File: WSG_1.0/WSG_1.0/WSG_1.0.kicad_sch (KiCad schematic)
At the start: 0 parts

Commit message: working on esp, power and signal done
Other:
- added sheet WSG_ADC (untitled.kicad_sch)
- added sheet WSG_ESP (WSG_ESP.kicad_sch)
- added sheet WSG_Power-Memory (WSG_ADC.kicad_sch)
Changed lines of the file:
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@@
 	(generator_version "10.0")
 	(paper "A4")
+	(sheet
+		(at 45.72 96.52)
+		(size 57.15 30.48)
+		(exclude_from_sim no)
+		(in_bom yes)
+		(on_board yes)
+		(dnp no)
+		(fields_autoplaced yes)
+		(stroke
+			(width 0.1524)
+			(type solid)
+		)
+		(fill
+			(color 0 0 0 0)
+		)
+		(property "Sheetname" "WSG_Power-Memory"
+			(at 45.72 95.8084 0)
+			(show_name no)
+			(do_not_autoplace no)
+			(effects
+				(font
+					(size 1.27 1.27)
+				)
+				(justify left bottom)
+			)
+		)
+		(property "Sheetfile" "WSG_ADC.kicad_sch"
+			(at 45.72 127.5846 0)
+			(show_name no)
+			(do_not_autoplace no)
+			(effects
+				(font
+					(size 1.27 1.27)
+				)
+				(justify left top)
+			)
+		)
+		(instances
+			(project "WSG_1.0"
+				(path "/cb65811d-b245-4002-a5a3-eef29f2c4ddb"
+					(page "4")
+				)
+			)
+		)
+	)
+	(sheet
+		(at 148.59 60.96)
+		(size 68.58 36.83)
+		(exclude_from_sim no)
+		(in_bom yes)
+		(on_board yes)
+		(dnp no)
+		(fields_autoplaced yes)
+		(stroke
+			(width 0.1524)
+			(type solid)
+		)
+		(fill
+			(color 0 0 0 0)
+		)
+		(property "Sheetname" "WSG_ESP"
+			(at 148.59 60.2484 0)
+			(show_name no)
+			(do_not_autoplace no)
+			(effects
+				(font
+					(size 1.27 1.27)
+				)
+				(justify left bottom)
+			)
+		)
+		(property "Sheetfile" "WSG_ESP.kicad_sch"
+			(at 148.59 98.3746 0)
+			(show_name no)
+			(do_not_autoplace no)
+			(effects
+				(font
+					(size 1.27 1.27)
+				)
+				(justify left top)
+			)
+		)
+		(instances
+			(project "WSG_1.0"
+				(path "/cb65811d-b245-4002-a5a3-eef29f2c4ddb"
+					(page "3")
+				)
+			)
+		)
+	)
+	(sheet
+		(at 54.61 57.15)
+		(size 54.61 29.21)
+		(exclude_from_sim no)
+		(in_bom yes)
+		(on_board yes)
+		(dnp no)
+		(fields_autoplaced yes)
+		(stroke
+			(width 0.1524)
+			(type solid)
+		)
+		(fill
+			(color 0 0 0 0)
+		)
+		(property "Sheetname" "WSG_ADC"
+			(at 54.61 56.4384 0)
+			(show_name no)
+			(do_not_autoplace no)
+			(effects
+				(font
+					(size 1.27 1.27)
+				)
+				(justify left bottom)
+			)
+		)
+		(property "Sheetfile" "untitled.kicad_sch"
+			(at 54.61 86.9446 0)
+			(show_name no)
+			(do_not_autoplace no)
+			(effects
+				(font
+					(size 1.27 1.27)
+				)
+				(justify left top)
+			)
+		)
+		(instances
+			(project "WSG_1.0"
+				(path "/cb65811d-b245-4002-a5a3-eef29f2c4ddb"
+					(page "2")
+				)
+			)
+		)
+	)
 	(sheet_instances
 		(path "/"

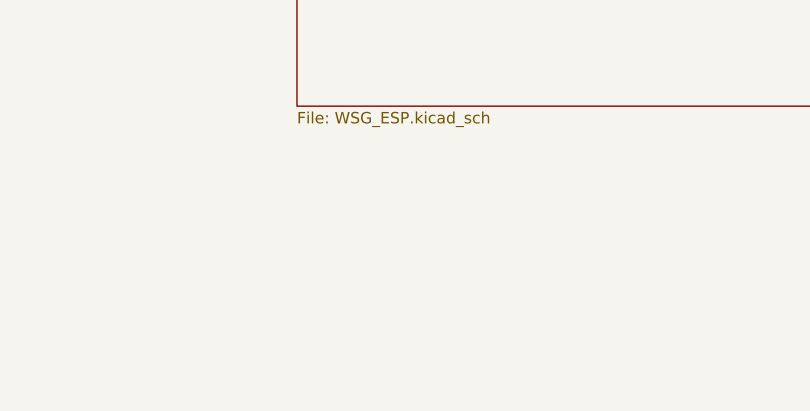
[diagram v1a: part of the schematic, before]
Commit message: added mounting holes, usb esd
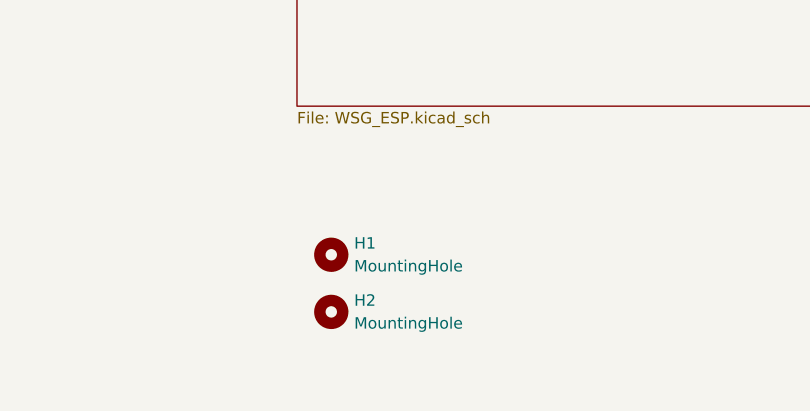
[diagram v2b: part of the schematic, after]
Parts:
- added H1, H2: MountingHole, symbol Mechanical:MountingHole
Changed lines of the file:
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@@
 	(generator_version "10.0")
 	(paper "A4")
+	(symbol
+		(lib_id "Mechanical:MountingHole")
+		(at 152.4 114.3 0)
+		(unit 1)
+		(body_style 1)
+		(exclude_from_sim no)
+		(in_bom no)
+		(on_board yes)
+		(in_pos_files yes)
+		(dnp no)
+		(fields_autoplaced yes)
+		(property "Reference" "H1"
+			(at 154.94 113.0299 0)
+			(show_name no)
+			(do_not_autoplace no)
+			(effects
+				(font
+					(size 1.27 1.27)
+				)
+				(justify left)
+			)
+		)
+		(property "Value" "MountingHole"
+			(at 154.94 115.5699 0)
+			(show_name no)
+			(do_not_autoplace no)
+			(effects
+				(font
+					(size 1.27 1.27)
+				)
+				(justify left)
+			)
+		)
+		(property "Footprint" ""
+			(at 152.4 114.3 0)
+			(hide yes)
+			(show_name no)
+			(do_not_autoplace no)
+			(effects
+				(font
+					(size 1.27 1.27)
+				)
+			)
+		)
+		(property "Datasheet" ""
+			(at 152.4 114.3 0)
+			(hide yes)
+			(show_name no)
+			(do_not_autoplace no)
+			(effects
+				(font
+					(size 1.27 1.27)
+				)
+			)
+		)
+		(property "Description" "Mounting Hole without connection"
+			(at 152.4 114.3 0)
+			(hide yes)
+			(show_name no)
+			(do_not_autoplace no)
+			(effects
+				(font
+					(size 1.27 1.27)
+				)
+			)
+		)
+		(instances
+			(project "WSG_1.0"
+				(path "/cb65811d-b245-4002-a5a3-eef29f2c4ddb"
+					(reference "H1")
+					(unit 1)
+				)
+			)
+		)
+	)
+	(symbol
+		(lib_id "Mechanical:MountingHole")
+		(at 152.4 120.65 0)
+		(unit 1)
+		(body_style 1)
+		(exclude_from_sim no)
+		(in_bom no)
+		(on_board yes)
+		(in_pos_files yes)
+		(dnp no)
+		(fields_autoplaced yes)
+		(property "Reference" "H2"
+			(at 154.94 119.3799 0)
+			(show_name no)
+			(do_not_autoplace no)
+			(effects
+				(font
+					(size 1.27 1.27)
+				)
+				(justify left)
+			)
+		)
+		(property "Value" "MountingHole"
+			(at 154.94 121.9199 0)
+			(show_name no)
+			(do_not_autoplace no)
+			(effects
+				(font
+					(size 1.27 1.27)
+				)
+				(justify left)
+			)
+		)
+		(property "Footprint" ""
+			(at 152.4 120.65 0)
+			(hide yes)
+			(show_name no)
+			(do_not_autoplace no)
+			(effects
+				(font
+					(size 1.27 1.27)
+				)
+			)
+		)
+		(property "Datasheet" ""
+			(at 152.4 120.65 0)
+			(hide yes)
+			(show_name no)
+			(do_not_autoplace no)
+			(effects
+				(font
+					(size 1.27 1.27)
+				)
+			)
+		)
+		(property "Description" "Mounting Hole without connection"
+			(at 152.4 120.65 0)
+			(hide yes)
+			(show_name no)
+			(do_not_autoplace no)
+			(effects
+				(font
+					(size 1.27 1.27)
+				)
+			)
+		)
+		(instances
+			(project "WSG_1.0"
+				(path "/cb65811d-b245-4002-a5a3-eef29f2c4ddb"
+					(reference "H2")
+					(unit 1)
+				)
+			)
+		)
+	)
 	(sheet
 		(at 45.72 96.52)

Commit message: forgot to commit, started layout and started implementing sophie's/cyan's feedback for the schematic
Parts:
- H1, H2: footprint (none) -> MountingHole:MountingHole_3.2mm_M3
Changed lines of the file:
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@@
 			)
 		)
-		(property "Footprint" ""
+		(property "Footprint" "MountingHole:MountingHole_3.2mm_M3"
 			(at 152.4 114.3 0)
 			(hide yes)
@@
 			)
 		)
-		(property "Footprint" ""
+		(property "Footprint" "MountingHole:MountingHole_3.2mm_M3"
 			(at 152.4 120.65 0)
 			(hide yes)

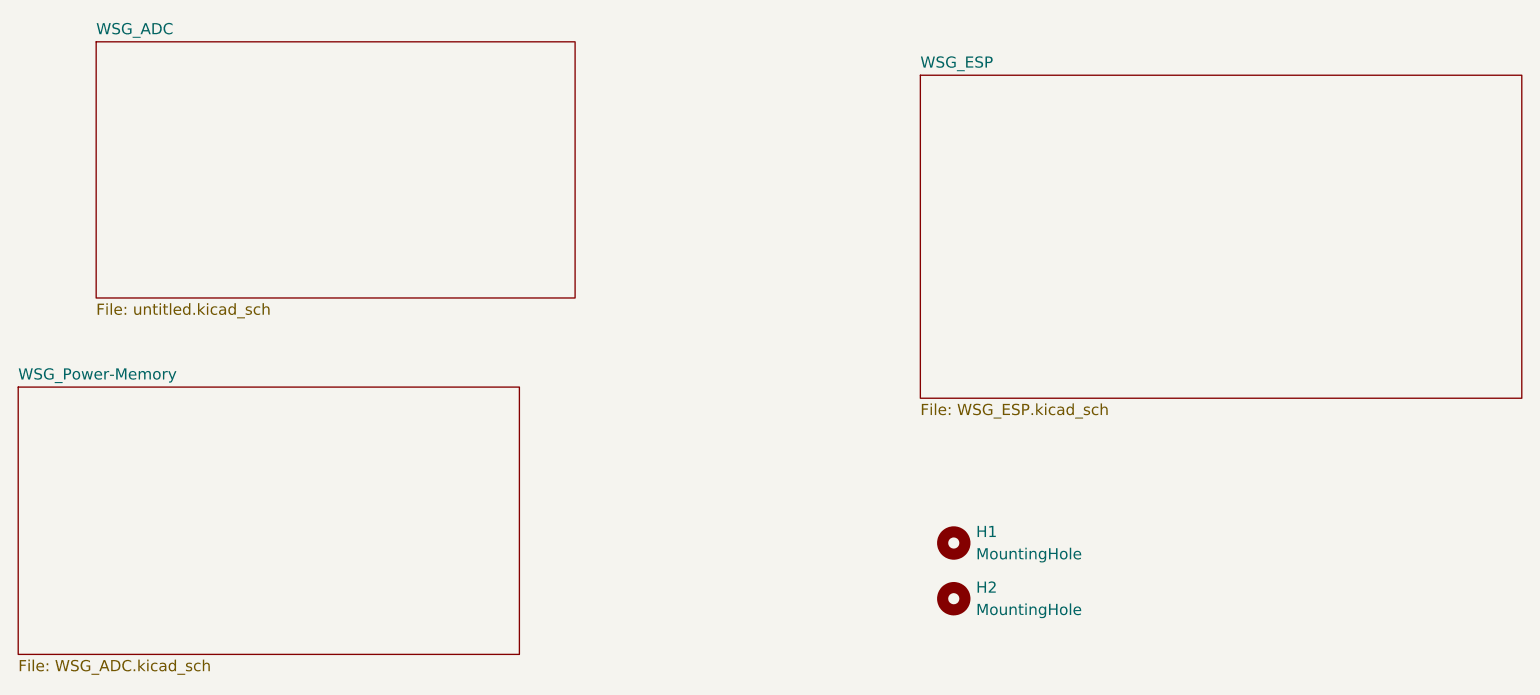
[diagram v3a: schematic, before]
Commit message: new layout started, clusters almost done
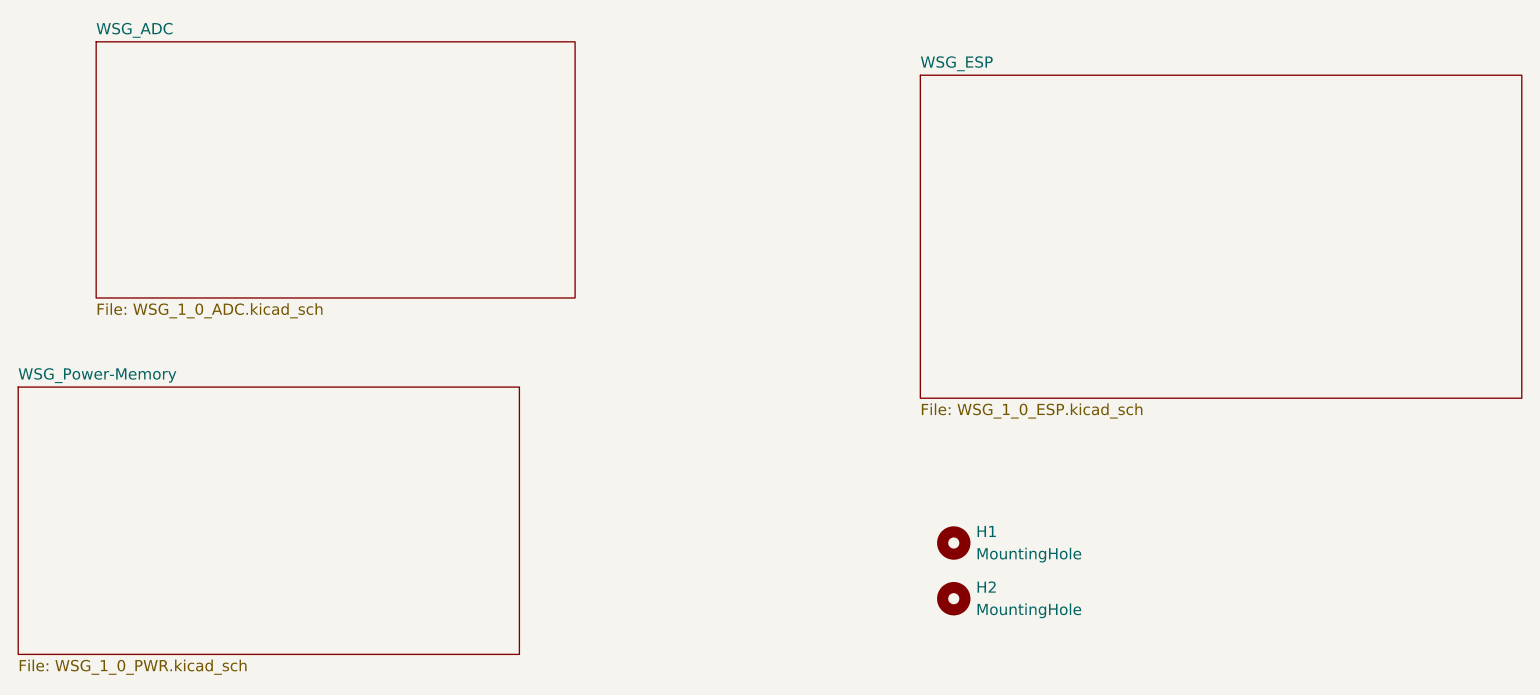
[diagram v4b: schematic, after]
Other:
- sheet WSG_ADC: file untitled.kicad_sch -> WSG_1_0_ADC.kicad_sch
- sheet WSG_ESP: file WSG_ESP.kicad_sch -> WSG_1_0_ESP.kicad_sch
- sheet WSG_Power-Memory: file WSG_ADC.kicad_sch -> WSG_1_0_PWR.kicad_sch
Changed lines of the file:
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@@
 			)
 		)
-		(property "Sheetfile" "WSG_ADC.kicad_sch"
+		(property "Sheetfile" "WSG_1_0_PWR.kicad_sch"
 			(at 45.72 127.5846 0)
 			(show_name no)
@@
 			)
 		)
-		(property "Sheetfile" "WSG_ESP.kicad_sch"
+		(property "Sheetfile" "WSG_1_0_ESP.kicad_sch"
 			(at 148.59 98.3746 0)
 			(show_name no)
@@
 			)
 		)
-		(property "Sheetfile" "untitled.kicad_sch"
+		(property "Sheetfile" "WSG_1_0_ADC.kicad_sch"
 			(at 54.61 86.9446 0)
 			(show_name no)
